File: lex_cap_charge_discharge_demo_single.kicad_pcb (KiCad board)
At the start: 2 copper layers, 38.1 x 40.6 mm, 14 parts, among them J1 +5V, J2 GND, J3 Conn_01x01_Socket, J4 Conn_01x01_Socket, SW1 charge, SW2 discharge

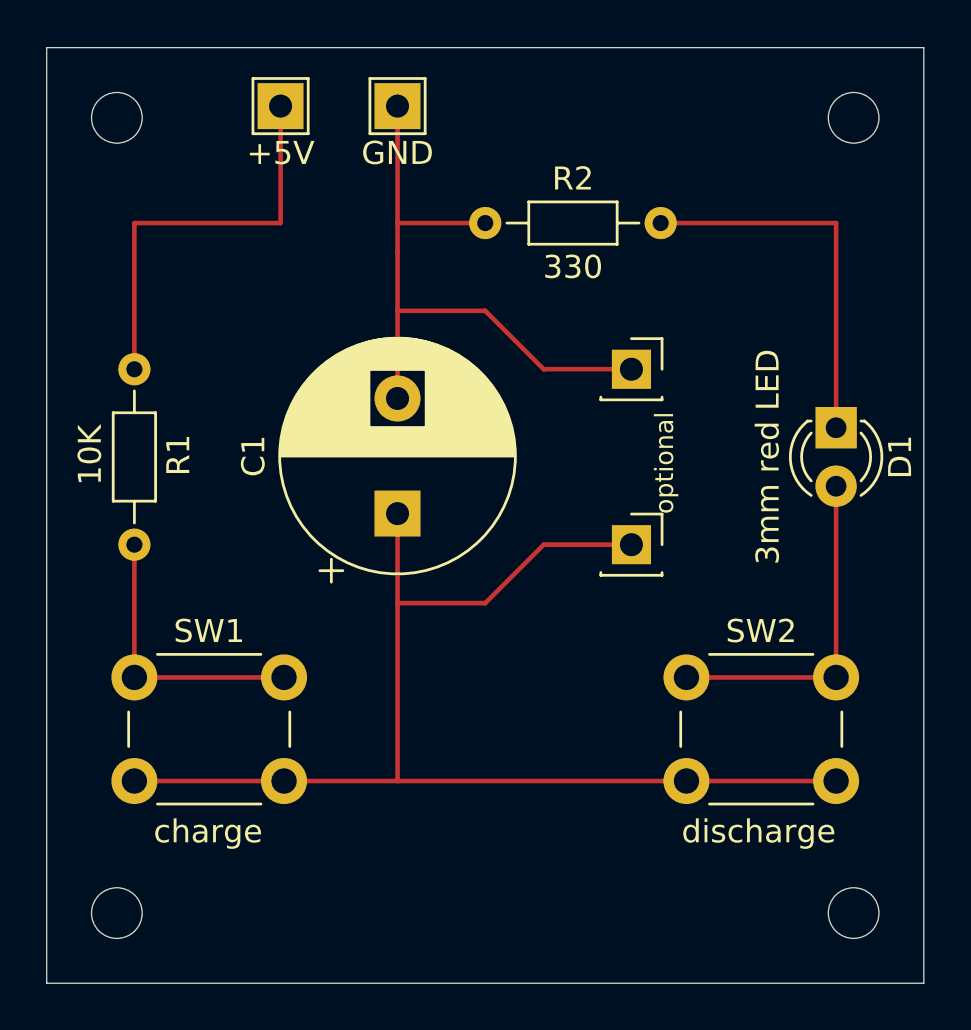
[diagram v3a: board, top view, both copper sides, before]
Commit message: add hunsley.io top of front, make optional headers closer to cap
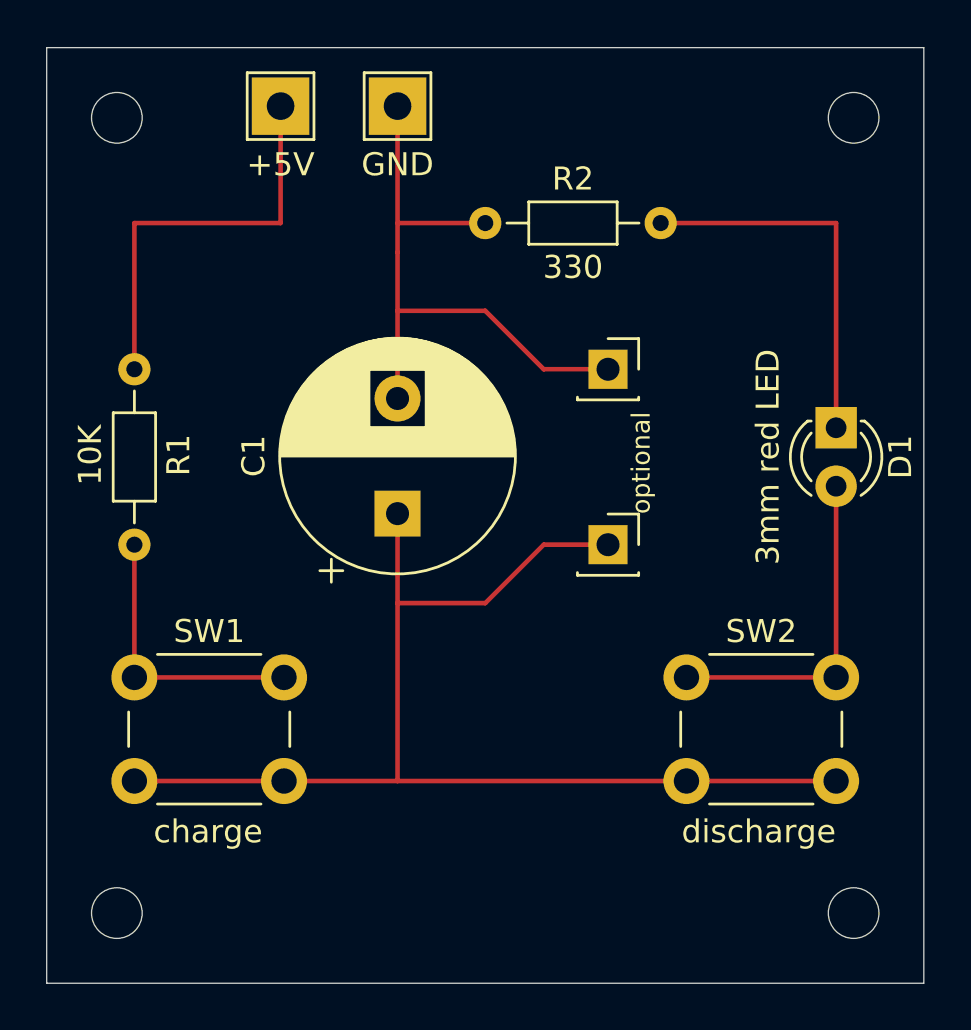
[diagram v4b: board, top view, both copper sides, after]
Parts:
- J1, J2: footprint TestPoint:TestPoint_THTPad_2.0x2.0mm_Drill1.0mm -> TestPoint:TestPoint_THTPad_2.5x2.5mm_Drill1.2mm
- moved J3 1.02 mm to (74.4, 71.6)
- moved J4 1.02 mm to (74.4, 64.0)
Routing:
- net Net-(J3-Pin_1): track 53.3 -> 52.3 mm
- net GND: track 27.7 -> 26.7 mm
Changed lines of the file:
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@@
 		)
 	)
-	(footprint "TestPoint:TestPoint_THTPad_2.0x2.0mm_Drill1.0mm"
+	(footprint "TestPoint:TestPoint_THTPad_2.5x2.5mm_Drill1.2mm"
 		(layer "F.Cu")
 		(at 60.1628 52.5842)
-		(descr "THT rectangular pad as test Point, square 2.0mm_Drill1.0mm  side length, hole diameter 1.0mm")
+		(descr "THT rectangular pad as test Point, square 2.5mm side length, hole diameter 1.2mm")
 		(tags "test point THT pad rectangle square")
 		(property "Reference" "J1"
-			(at 0 -1.998 0)
-			(layer "User.1")
+			(at 0 -2.148 0)
+			(layer "F.SilkS")
+			(hide yes)
 			(effects
 				(font
@@
 		)
 		(property "Value" "+5V"
-			(at 0 2.05 0)
+			(at 0 2.54 0)
 			(layer "F.SilkS")
 			(effects
@@
 		(attr exclude_from_pos_files)
 		(fp_line
-			(start -1.2 -1.2)
-			(end 1.2 -1.2)
-			(stroke
-				(width 0.12)
-				(type solid)
-			)
-			(layer "F.SilkS")
-		)
-		(fp_line
-			(start -1.2 1.2)
-			(end -1.2 -1.2)
-			(stroke
-				(width 0.12)
-				(type solid)
-			)
-			(layer "F.SilkS")
-		)
-		(fp_line
-			(start 1.2 -1.2)
-			(end 1.2 1.2)
-			(stroke
-				(width 0.12)
-				(type solid)
-			)
-			(layer "F.SilkS")
-		)
-		(fp_line
-			(start 1.2 1.2)
-			(end -1.2 1.2)
-			(stroke
-				(width 0.12)
-				(type solid)
-			)
-			(layer "F.SilkS")
-		)
-		(fp_line
-			(start -1.5 -1.5)
-			(end -1.5 1.5)
-			(stroke
-				(width 0.05)
-				(type solid)
-			)
-			(layer "F.CrtYd")
-		)
-		(fp_line
-			(start -1.5 -1.5)
-			(end 1.5 -1.5)
-			(stroke
-				(width 0.05)
-				(type solid)
-			)
-			(layer "F.CrtYd")
-		)
-		(fp_line
-			(start 1.5 1.5)
-			(end -1.5 1.5)
-			(stroke
-				(width 0.05)
-				(type solid)
-			)
-			(layer "F.CrtYd")
-		)
-		(fp_line
-			(start 1.5 1.5)
-			(end 1.5 -1.5)
+			(start -1.45 -1.45)
+			(end 1.45 -1.45)
+			(stroke
+				(width 0.12)
+				(type solid)
+			)
+			(layer "F.SilkS")
+		)
+		(fp_line
+			(start -1.45 1.45)
+			(end -1.45 -1.45)
+			(stroke
+				(width 0.12)
+				(type solid)
+			)
+			(layer "F.SilkS")
+		)
+		(fp_line
+			(start 1.45 -1.45)
+			(end 1.45 1.45)
+			(stroke
+				(width 0.12)
+				(type solid)
+			)
+			(layer "F.SilkS")
+		)
+		(fp_line
+			(start 1.45 1.45)
+			(end -1.45 1.45)
+			(stroke
+				(width 0.12)
+				(type solid)
+			)
+			(layer "F.SilkS")
+		)
+		(fp_line
+			(start -1.75 -1.75)
+			(end -1.75 1.75)
+			(stroke
+				(width 0.05)
+				(type solid)
+			)
+			(layer "F.CrtYd")
+		)
+		(fp_line
+			(start -1.75 -1.75)
+			(end 1.75 -1.75)
+			(stroke
+				(width 0.05)
+				(type solid)
+			)
+			(layer "F.CrtYd")
+		)
+		(fp_line
+			(start 1.75 1.75)
+			(end -1.75 1.75)
+			(stroke
+				(width 0.05)
+				(type solid)
+			)
+			(layer "F.CrtYd")
+		)
+		(fp_line
+			(start 1.75 1.75)
+			(end 1.75 -1.75)
 			(stroke
 				(width 0.05)
@@
 		)
 		(fp_text user "${REFERENCE}"
-			(at 0 -2 0)
-			(layer "User.1")
+			(at 0 -2.15 0)
+			(layer "F.Fab")
 			(effects
 				(font
@@
 		(pad "1" thru_hole rect
 			(at 0 0)
-			(size 2 2)
-			(drill 1)
+			(size 2.5 2.5)
+			(drill 1.2)
 			(layers "*.Cu" "*.Mask")
 			(remove_unused_layers no)
@@
 	(footprint "Connector_PinSocket_2.54mm:PinSocket_1x01_P2.54mm_Vertical"
 		(layer "F.Cu")
-		(at 75.4028 71.6342)
+		(at 74.3868 71.6342)
 		(descr "Through hole straight socket strip, 1x01, 2.54mm pitch, single row (from Kicad 4.0.7), script generated")
 		(tags "Through hole socket strip THT 1x01 2.54mm single row")
@@
 		(embedded_fonts no)
 	)
-	(footprint "TestPoint:TestPoint_THTPad_2.0x2.0mm_Drill1.0mm"
+	(footprint "TestPoint:TestPoint_THTPad_2.5x2.5mm_Drill1.2mm"
 		(layer "F.Cu")
 		(at 65.2428 52.5842)
-		(descr "THT rectangular pad as test Point, square 2.0mm_Drill1.0mm  side length, hole diameter 1.0mm")
+		(descr "THT rectangular pad as test Point, square 2.5mm side length, hole diameter 1.2mm")
 		(tags "test point THT pad rectangle square")
 		(property "Reference" "J2"
-			(at 0 -1.998 0)
-			(layer "User.1")
+			(at 0 -2.148 0)
+			(layer "F.SilkS")
+			(hide yes)
 			(effects
 				(font
@@
 		)
 		(property "Value" "GND"
-			(at 0 2.05 0)
+			(at 0 2.54 0)
 			(layer "F.SilkS")
 			(effects
@@
 		(attr exclude_from_pos_files)
 		(fp_line
-			(start -1.2 -1.2)
-			(end 1.2 -1.2)
-			(stroke
-				(width 0.12)
-				(type solid)
-			)
-			(layer "F.SilkS")
-		)
-		(fp_line
-			(start -1.2 1.2)
-			(end -1.2 -1.2)
-			(stroke
-				(width 0.12)
-				(type solid)
-			)
-			(layer "F.SilkS")
-		)
-		(fp_line
-			(start 1.2 -1.2)
-			(end 1.2 1.2)
-			(stroke
-				(width 0.12)
-				(type solid)
-			)
-			(layer "F.SilkS")
-		)
-		(fp_line
-			(start 1.2 1.2)
-			(end -1.2 1.2)
-			(stroke
-				(width 0.12)
-				(type solid)
-			)
-			(layer "F.SilkS")
-		)
-		(fp_line
-			(start -1.5 -1.5)
-			(end -1.5 1.5)
-			(stroke
-				(width 0.05)
-				(type solid)
-			)
-			(layer "F.CrtYd")
-		)
-		(fp_line
-			(start -1.5 -1.5)
-			(end 1.5 -1.5)
-			(stroke
-				(width 0.05)
-				(type solid)
-			)
-			(layer "F.CrtYd")
-		)
-		(fp_line
-			(start 1.5 1.5)
-			(end -1.5 1.5)
-			(stroke
-				(width 0.05)
-				(type solid)
-			)
-			(layer "F.CrtYd")
-		)
-		(fp_line
-			(start 1.5 1.5)
-			(end 1.5 -1.5)
+			(start -1.45 -1.45)
+			(end 1.45 -1.45)
+			(stroke
+				(width 0.12)
+				(type solid)
+			)
+			(layer "F.SilkS")
+		)
+		(fp_line
+			(start -1.45 1.45)
+			(end -1.45 -1.45)
+			(stroke
+				(width 0.12)
+				(type solid)
+			)
+			(layer "F.SilkS")
+		)
+		(fp_line
+			(start 1.45 -1.45)
+			(end 1.45 1.45)
+			(stroke
+				(width 0.12)
+				(type solid)
+			)
+			(layer "F.SilkS")
+		)
+		(fp_line
+			(start 1.45 1.45)
+			(end -1.45 1.45)
+			(stroke
+				(width 0.12)
+				(type solid)
+			)
+			(layer "F.SilkS")
+		)
+		(fp_line
+			(start -1.75 -1.75)
+			(end -1.75 1.75)
+			(stroke
+				(width 0.05)
+				(type solid)
+			)
+			(layer "F.CrtYd")
+		)
+		(fp_line
+			(start -1.75 -1.75)
+			(end 1.75 -1.75)
+			(stroke
+				(width 0.05)
+				(type solid)
+			)
+			(layer "F.CrtYd")
+		)
+		(fp_line
+			(start 1.75 1.75)
+			(end -1.75 1.75)
+			(stroke
+				(width 0.05)
+				(type solid)
+			)
+			(layer "F.CrtYd")
+		)
+		(fp_line
+			(start 1.75 1.75)
+			(end 1.75 -1.75)
 			(stroke
 				(width 0.05)
@@
 		)
 		(fp_text user "${REFERENCE}"
-			(at 0 -2 0)
-			(layer "User.1")
+			(at 0 -2.15 0)
+			(layer "F.Fab")
 			(effects
 				(font
@@
 		(pad "1" thru_hole rect
 			(at 0 0)
-			(size 2 2)
-			(drill 1)
+			(size 2.5 2.5)
+			(drill 1.2)
 			(layers "*.Cu" "*.Mask")
 			(remove_unused_layers no)
@@
 	(footprint "Connector_PinSocket_2.54mm:PinSocket_1x01_P2.54mm_Vertical"
 		(layer "F.Cu")
-		(at 75.4028 64.0142)
+		(at 74.3868 64.0142)
 		(descr "Through hole straight socket strip, 1x01, 2.54mm pitch, single row (from Kicad 4.0.7), script generated")
 		(tags "Through hole socket strip THT 1x01 2.54mm single row")
@@
 	)
 	(gr_text "optional"
-		(at 77.3078 70.3042 90)
+		(at 76.2918 70.3042 90)
 		(layer "F.SilkS")
 		(effects
@@
 			(font
 				(size 2 2)
+				(thickness 0.15)
+			)
+			(justify top)
+		)
+		(border no)
+		(stroke
+			(width 0)
+			(type solid)
+		)
+	)
+	(gr_text_box "hunsley.io"
+		(start 68.1928 50.6905)
+		(end 82.1048 53.7159)
+		(margins 1.0025 1.0025 1.0025 1.0025)
+		(layer "F.SilkS")
+		(effects
+			(font
+				(size 1.5 1.5)
 				(thickness 0.15)
 			)
@@
 	(segment
 		(start 71.5928 71.6342)
+		(end 74.3868 71.6342)
+		(width 0.2)
+		(layer "F.Cu")
+		(net 2)
+	)
+	(segment
+		(start 71.5928 71.6342)
 		(end 69.0528 74.1742)
 		(width 0.2)
@@
 	)
 	(segment
-		(start 75.4028 71.6342)
-		(end 71.5928 71.6342)
-		(width 0.2)
-		(layer "F.Cu")
-		(net 2)
-	)
-	(segment
 		(start 76.6728 57.6642)
 		(end 84.2928 57.6642)
@@
 	)
 	(segment
-		(start 75.4028 64.0142)
-		(end 71.5928 64.0142)
-		(width 0.2)
-		(layer "F.Cu")
+		(start 71.5928 64.0142)
+		(end 74.3868 64.0142)
+		(width 0.2)
+		(layer "F.Cu")
